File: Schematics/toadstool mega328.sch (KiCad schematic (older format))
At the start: 25 parts, among them CON1 BARREL_JACK, IC1 ATMEGA328P-P, K1 SHIELD, K2 V-SELECT, K4 ICSP, K5 PIN 2-8, K6 PIN 21-28, K7 XTAL, K8 PIN 15-19, K9 PIN 11-14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

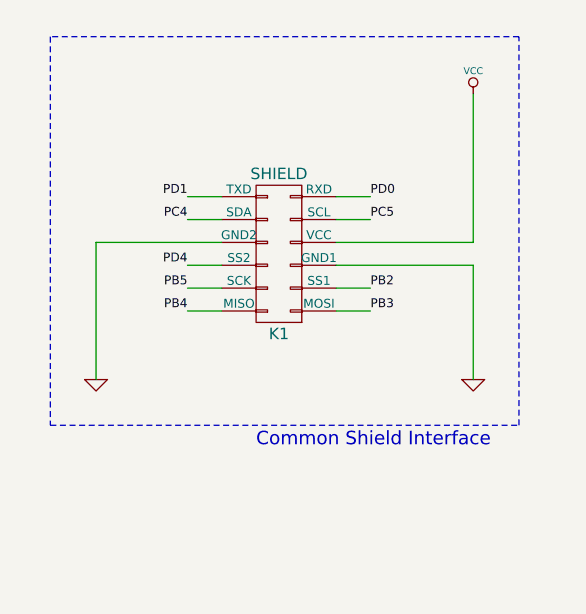
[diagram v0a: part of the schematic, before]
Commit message: Version 0.2 - Updates from v0.1 prototype
Final changes from v0.1 prototype:
- Add aluminium caps
- Silkscreen cosmetics
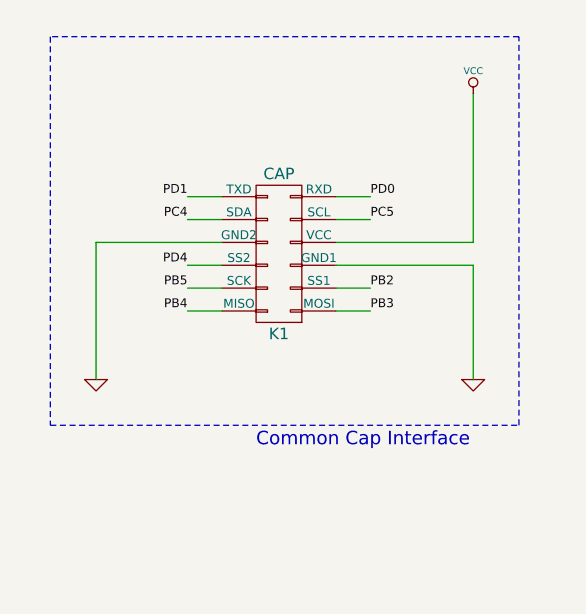
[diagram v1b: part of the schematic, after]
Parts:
- C1, C2: footprint Capacitors_Tantalum_SMD:TantalC_SizeA_EIA-3216_HandSoldering -> toadstool:c_elec_4x5.3
- D2: footprint LEDs:LED-0805 -> Toadstool:LED-0805
- K1: value SHIELD -> CAP
- K4: footprint Pin_Headers:Pin_Header_Straight_2x03 -> Toadstool:ICSP_Header_2x03
- R1, R2, R3, R4, R5: footprint Resistors_SMD:R_0805_HandSoldering -> Resistors_SMD:R_0805
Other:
- note added: "Common Cap Interface"
- note removed: "Common Shield Interface"
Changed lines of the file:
@@
 P 9950 1750
 F 0 "K1" H 9950 2100 50  0000 C CNN
-F 1 "SHIELD" H 9950 1400 50  0000 C CNN
+F 1 "CAP" H 9950 1400 50  0000 C CNN
 F 2 "Socket_Strips:Socket_Strip_Straight_2x06" H 9950 550 60  0001 C CNN
 F 3 "" H 9950 550 60  0000 C CNN
@@
 F 0 "K4" H 8200 3350 50  0000 C CNN
 F 1 "ICSP" H 8200 2950 50  0000 C CNN
-F 2 "Pin_Headers:Pin_Header_Straight_2x03" H 8200 1950 60  0001 C CNN
+F 2 "Toadstool:ICSP_Header_2x03" H 8200 1950 60  0001 C CNN
 F 3 "" H 8200 1950 60  0000 C CNN
 	1    8200 3150
@@
 F 0 "C1" H 3600 1450 50  0000 L CNN
 F 1 "10uF" H 3600 1250 50  0000 L CNN
-F 2 "Capacitors_Tantalum_SMD:TantalC_SizeA_EIA-3216_HandSoldering" H 3550 1350 60  0001 C CNN
+F 2 "toadstool:c_elec_4x5.3" H 3550 1350 60  0001 C CNN
 F 3 "" H 3550 1350 60  0000 C CNN
 	1    3550 1350
@@
 F 0 "C2" H 5500 1450 50  0000 L CNN
 F 1 "10uF" H 5500 1250 50  0000 L CNN
-F 2 "Capacitors_Tantalum_SMD:TantalC_SizeA_EIA-3216_HandSoldering" H 5450 1350 60  0001 C CNN
+F 2 "toadstool:c_elec_4x5.3" H 5450 1350 60  0001 C CNN
 F 3 "" H 5450 1350 60  0000 C CNN
 	1    5450 1350
@@
 F 0 "D2" H 6400 1500 50  0000 C CNN
 F 1 "PWR" H 6400 1300 50  0000 C CNN
-F 2 "LEDs:LED-0805" H 6400 1400 60  0001 C CNN
+F 2 "Toadstool:LED-0805" H 6400 1400 60  0001 C CNN
 F 3 "" H 6400 1400 60  0000 C CNN
 	1    6400 1400
@@
 F 0 "R1" V 6130 1150 40  0000 C CNN
 F 1 "R" V 6057 1151 40  0000 C CNN
-F 2 "Resistors_SMD:R_0805_HandSoldering" V 5980 1150 30  0001 C CNN
+F 2 "Resistors_SMD:R_0805" V 5980 1150 30  0001 C CNN
 F 3 "" H 6050 1150 30  0000 C CNN
 	1    6050 1150
@@
 F 0 "R3" V 4580 1850 40  0000 C CNN
 F 1 "200R" V 4507 1851 40  0000 C CNN
-F 2 "Resistors_SMD:R_0805_HandSoldering" V 4430 1850 30  0001 C CNN
+F 2 "Resistors_SMD:R_0805" V 4430 1850 30  0001 C CNN
 F 3 "" H 4500 1850 30  0000 C CNN
 	1    4500 1850
@@
 F 0 "R2" V 4980 1400 40  0000 C CNN
 F 1 "120R" V 4907 1401 40  0000 C CNN
-F 2 "Resistors_SMD:R_0805_HandSoldering" V 4830 1400 30  0001 C CNN
+F 2 "Resistors_SMD:R_0805" V 4830 1400 30  0001 C CNN
 F 3 "" H 4900 1400 30  0000 C CNN
 	1    4900 1400
@@
 F 0 "R4" V 4580 2050 40  0000 C CNN
 F 1 "360R" V 4507 2051 40  0000 C CNN
-F 2 "Resistors_SMD:R_0805_HandSoldering" V 4430 2050 30  0001 C CNN
+F 2 "Resistors_SMD:R_0805" V 4430 2050 30  0001 C CNN
 F 3 "" H 4500 2050 30  0000 C CNN
 	1    4500 2050
@@
 F 0 "R5" V 6130 5100 40  0000 C CNN
 F 1 "10k" V 6057 5101 40  0000 C CNN
-F 2 "Resistors_SMD:R_0805_HandSoldering" V 5980 5100 30  0001 C CNN
+F 2 "Resistors_SMD:R_0805" V 5980 5100 30  0001 C CNN
 F 3 "" H 6050 5100 30  0000 C CNN
 	1    6050 5100
@@
 	8950 2500 11000 2500
 Text Notes 9850 2600 0    59   ~ 0
-Common Shield Interface
+Common Cap Interface
 Text Label 3250 4100 2    39   ~ 0
 AREF
